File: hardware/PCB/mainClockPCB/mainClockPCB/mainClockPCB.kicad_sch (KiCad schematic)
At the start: 51 parts, among them IC2 SPX1117M3-L_TR, IC3 MCP7940N-I_P, IC4 PAM8904QJER, J1 USB_C_Receptacle_USB2.0_16P, J2 Conn_01x09_Socket, J3 Conn_01x02_Socket, J4 Conn_01x09_Socket, J5 Conn_01x06, SW1 SW_Push, SW2 SW_Push, SW3 SW_Push, SW4 SW_Push, U1 PEC11R-4320K-S0012, U2 USBLC6-2SC6, U3 ESP32-S3-WROOM-2, U4 74HC165, Y1 AB26T-32.768KHZ-6

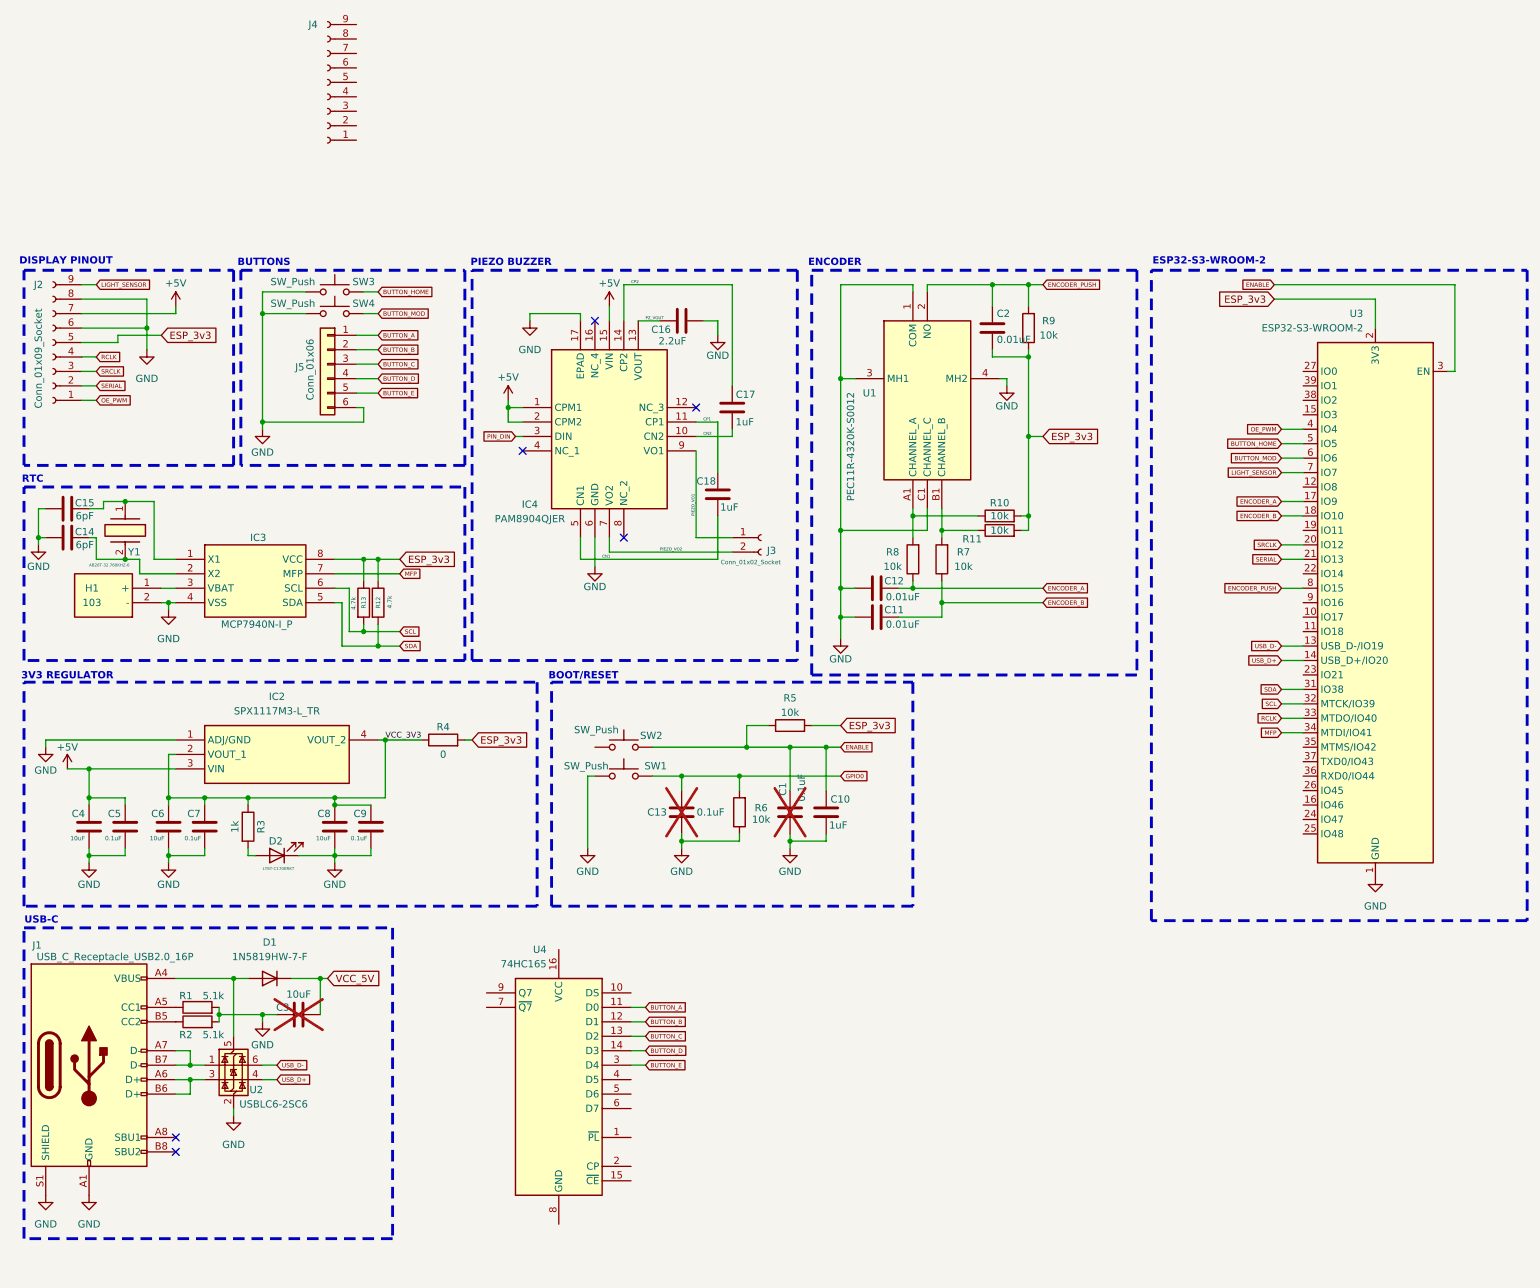
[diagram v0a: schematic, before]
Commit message: expansion/debug/jtag/strap headers
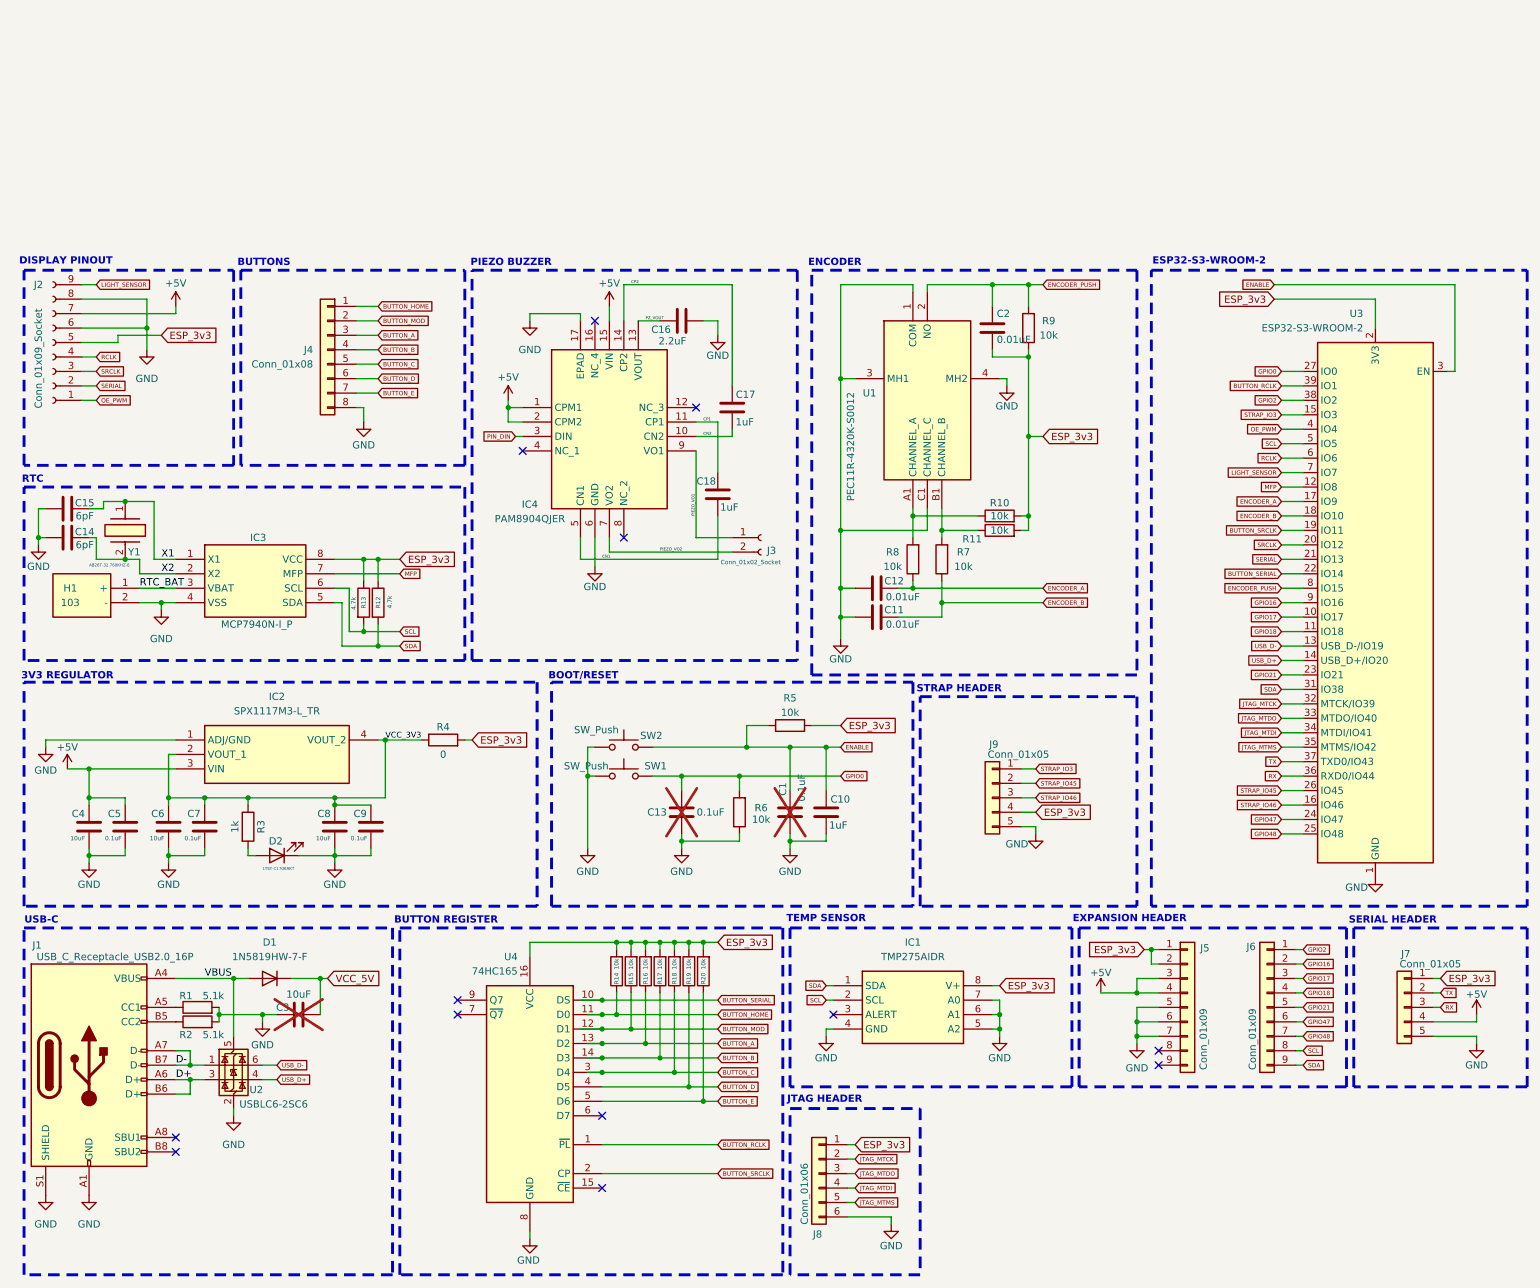
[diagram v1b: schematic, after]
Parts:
- removed J4: Conn_01x09_Socket, Connector_JST:JST_XH_B9B-XH-A_1x09_P2.50mm_Vertical, symbol Connector:Conn_01x09_Socket
- removed J5: Conn_01x06, symbol Connector_Generic:Conn_01x06
- removed SW3, SW4: SW_Push, Button_Switch_THT:SW_PUSH_6mm_H5mm, symbol Switch:SW_Push
- added IC1: TMP275AIDR, SamacSys_Parts:SOIC127P600X175-8N, symbol SamacSys_Parts:TMP275AIDR
- added J4: Conn_01x08, Connector_PinSocket_2.54mm:PinSocket_1x08_P2.54mm_Vertical, symbol Connector_Generic:Conn_01x08
- added J5, J6: Conn_01x09, Connector_PinSocket_2.54mm:PinSocket_1x09_P2.54mm_Vertical, symbol Connector_Generic:Conn_01x09
- added J7, J9: Conn_01x05, Connector_PinSocket_2.54mm:PinSocket_1x05_P2.54mm_Vertical, symbol Connector_Generic:Conn_01x05
- added J8: Conn_01x06, Connector_PinSocket_2.54mm:PinSocket_1x06_P2.54mm_Vertical, symbol Connector_Generic:Conn_01x06
- added R14, R15, R16, R17, R18, R19, R20: 10k, Resistor_SMD:R_0603_1608Metric_Pad0.98x0.95mm_HandSolder, symbol Device:R
- J3: footprint Connector_PinHeader_2.54mm:PinHeader_1x02_P2.54mm_Vertical -> Connector_PinSocket_2.54mm:PinSocket_1x02_P2.54mm_Vertical
- U4: footprint (none) -> Package_DIP:DIP-16_W7.62mm_Socket
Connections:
- net +5V: now also J5.3 (Pin_3), J5.4 (Pin_4), J7.4 (Pin_4)
- net BUTTON_A: now also U4.13 (D2), J4.3 (Pin_3), R16.1; no longer U4.11 (D0)
- net BUTTON_B: now also U4.14 (D3), J4.4 (Pin_4), R17.1; no longer U4.12 (D1)
- net BUTTON_C: now also U4.3 (D4), J4.5 (Pin_5), R18.1; no longer U4.13 (D2)
- net BUTTON_D: now also U4.4 (D5), J4.6 (Pin_6), R19.1; no longer U4.14 (D3)
- net BUTTON_E: now also U4.5 (D6), J4.7 (Pin_7), R20.1; no longer U4.3 (D4)
- net BUTTON_HOME: now also U4.11 (D0), J4.1 (Pin_1), R14.1; no longer U3.5 (IO5)
- net BUTTON_MOD: now also U4.12 (D1), J4.2 (Pin_2), R15.1; no longer U3.6 (IO6)
- net ESP_3v3: now also U4.16 (VCC), IC1.8 (V+), J5.1 (Pin_1), J5.2 (Pin_2), J7.1 (Pin_1), J8.1 (Pin_1), J9.4 (Pin_4), R14.2, R15.2, R16.2, R17.2, R18.2, R19.2, R20.2
- net GND: now also SW2.1, U4.8 (GND), IC1.4 (GND), IC1.5 (A2), IC1.6 (A1), IC1.7 (A0), J4.8 (Pin_8), J5.5 (Pin_5), J5.6 (Pin_6), J5.7 (Pin_7), J7.5 (Pin_5), J8.6 (Pin_6), J9.5 (Pin_5)
- net GPIO0: now also U3.27 (IO0)
- net MFP: now also U3.12 (IO8); no longer U3.34 (MTDI/IO41)
- net RCLK: now also U3.6 (IO6); no longer U3.33 (MTDO/IO40)
- net SCL: now also U3.5 (IO5), IC1.2 (SCL), J6.8 (Pin_8); no longer U3.32 (MTCK/IO39)
- net SDA: now also IC1.1 (SDA), J6.9 (Pin_9)
- net VBUS: now reaches D1.2 (A), J1.A4 (VBUS), J1.A9 (VBUS), J1.B4 (VBUS), J1.B9 (VBUS), U2.5 (VBUS)
- net X1: now reaches C15.2, IC3.1 (X1), Y1.1
- net X2: now reaches C14.2, IC3.2 (X2), Y1.2
- net RTC_BAT: now reaches H1.1 (+), IC3.3 (VBAT)
- net D+: now reaches J1.A6 (D+), J1.B6 (D+), U2.3 (I/O2)
- net D-: now reaches J1.A7 (D-), J1.B7 (D-), U2.1 (I/O1)
- net GPIO17: now reaches U3.10 (IO17)
- net GPIO17: now also J6.3 (Pin_3)
- net GPIO18: now reaches U3.11 (IO18)
- net GPIO18: now also J6.4 (Pin_4)
- net STRAP_IO3: now reaches U3.15 (IO3)
- net STRAP_IO3: now also J9.1 (Pin_1)
- net STRAP_IO46: now reaches U3.16 (IO46)
- net STRAP_IO46: now also J9.3 (Pin_3)
- net BUTTON_SRCLK: now reaches U3.19 (IO11)
- net BUTTON_SRCLK: now also U4.2 (CP)
- net BUTTON_SERIAL: now reaches U3.22 (IO14)
- net BUTTON_SERIAL: now also U4.10 (DS)
- net GPIO21: now reaches U3.23 (IO21)
- net GPIO21: now also J6.5 (Pin_5)
- net GPIO47: now reaches U3.24 (IO47)
- net GPIO47: now also J6.6 (Pin_6)
- net GPIO48: now reaches U3.25 (IO48)
- net GPIO48: now also J6.7 (Pin_7)
- net STRAP_IO45: now reaches U3.26 (IO45)
- net STRAP_IO45: now also J9.2 (Pin_2)
- net JTAG_MTMS: now reaches U3.35 (MTMS/IO42)
- net JTAG_MTMS: now also J8.5 (Pin_5)
- net RX: now reaches U3.36 (RXD0/IO44)
- net RX: now also J7.3 (Pin_3)
- net TX: now reaches U3.37 (TXD0/IO43)
- net TX: now also J7.2 (Pin_2)
- net GPIO2: now reaches U3.38 (IO2)
- net GPIO2: now also J6.1 (Pin_1)
- net BUTTON_RCLK: now reaches U3.39 (IO1)
- net BUTTON_RCLK: now also U4.1 (~{PL})
- net GPIO16: now reaches U3.9 (IO16)
- net GPIO16: now also J6.2 (Pin_2)
- new net JTAG_MTCK: J8.2 (Pin_2), U3.32 (MTCK/IO39)
- new net JTAG_MTDI: J8.4 (Pin_4), U3.34 (MTDI/IO41)
- new net JTAG_MTDO: J8.3 (Pin_3), U3.33 (MTDO/IO40)
- no-connect marks 6 -> 13
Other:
- note added: "BUTTON REGISTER"
- note added: "EXPANSION HEADER"
- note added: "JTAG HEADER"
- note added: "SERIAL HEADER"
- note added: "STRAP HEADER"
- note added: "TEMP SENSOR"
- company: (none) -> NATHANIEL KESSEL
- moved on the sheet: H1, U4
